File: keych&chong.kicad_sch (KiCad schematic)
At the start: 104 parts

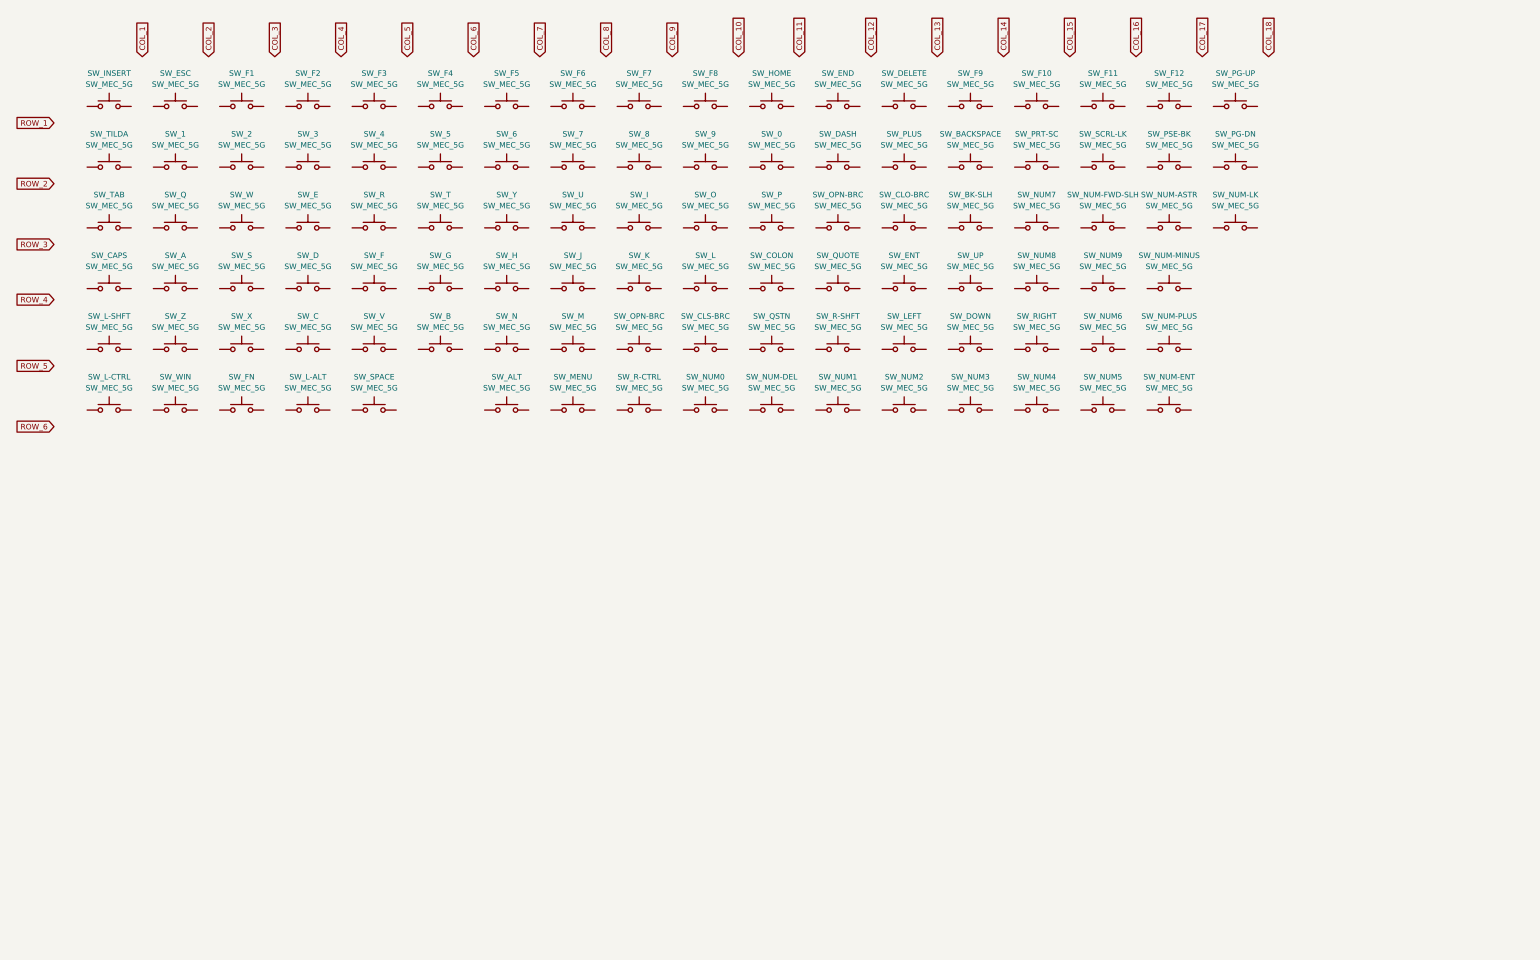
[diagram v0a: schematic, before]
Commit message: add connections to matrix schematic
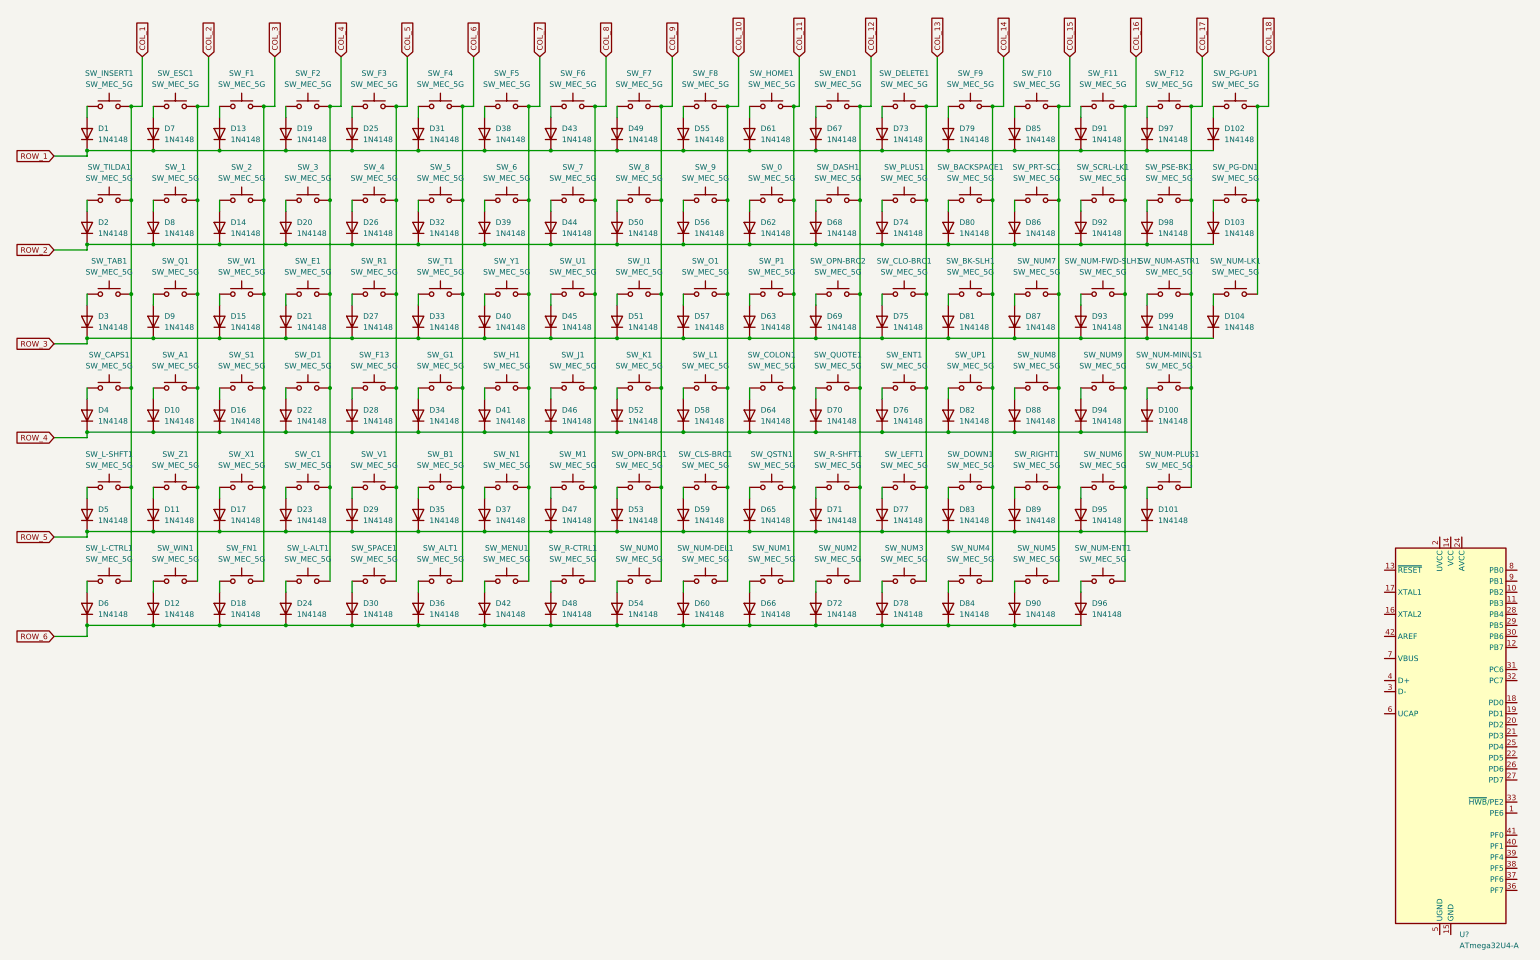
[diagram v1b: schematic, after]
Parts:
- added D1, D10, D100, D101, D102, D103, D104, D11, D12, D13, D14, D15, D16, D17, D18, D19, D2, D20, D21, D22, D23, D24, D25, D26, D27, D28, D29, D3, D30, D31, D32, D33, D34, D35, D36, D37, D38, D39, D4, D40, D41, D42, D43, D44, D45, D46, D47, D48, D49, D5, D50, D51, D52, D53, D54, D55, D56, D57, D58, D59, D6, D60, D61, D62, D63, D64, D65, D66, D67, D68, D69, D7, D70, D71, D72, D73, D74, D75, D76, D77, D78, D79, D8, D80, D81, D82, D83, D84, D85, D86, D87, D88, D89, D9, D90, D91, D92, D93, D94, D95, D96, D97, D98, D99: 1N4148, Diode_THT:D_DO-35_SOD27_P7.62mm_Horizontal, symbol Diode:1N4148
- added U?: ATmega32U4-A, Package_QFP:TQFP-44_10x10mm_P0.8mm, symbol MCU_Microchip_ATmega:ATmega32U4-A
- renumbered SW_A to SW_A1, SW_ALT to SW_ALT1, SW_B to SW_B1, SW_BACKSPACE to SW_BACKSPACE1, SW_BK-SLH to SW_BK-SLH1, SW_C to SW_C1, SW_CAPS to SW_CAPS1, SW_CLO-BRC to SW_CLO-BRC1, SW_CLS-BRC to SW_CLS-BRC1, SW_COLON to SW_COLON1, SW_D to SW_D1, SW_DASH to SW_DASH1, SW_DELETE to SW_DELETE1, SW_DOWN to SW_DOWN1, SW_E to SW_E1, SW_END to SW_END1, SW_ENT to SW_ENT1, SW_ESC to SW_ESC1, SW_F to SW_F13, SW_FN to SW_FN1, SW_G to SW_G1, SW_H to SW_H1, SW_HOME to SW_HOME1, SW_I to SW_I1, SW_INSERT to SW_INSERT1, SW_J to SW_J1, SW_K to SW_K1, SW_L-ALT to SW_L-ALT1, SW_L-CTRL to SW_L-CTRL1, SW_L-SHFT to SW_L-SHFT1, SW_L to SW_L1, SW_LEFT to SW_LEFT1, SW_M to SW_M1, SW_MENU to SW_MENU1, SW_N to SW_N1, SW_NUM-ASTR to SW_NUM-ASTR1, SW_NUM-DEL to SW_NUM-DEL1, SW_NUM-ENT to SW_NUM-ENT1, SW_NUM-FWD-SLH to SW_NUM-FWD-SLH1, SW_NUM-LK to SW_NUM-LK1, SW_NUM-MINUS to SW_NUM-MINUS1, SW_NUM-PLUS to SW_NUM-PLUS1, SW_O to SW_O1, SW_OPN-BRC to SW_OPN-BRC1, SW_OPN-BRC to SW_OPN-BRC2, SW_P to SW_P1, SW_PG-DN to SW_PG-DN1, SW_PG-UP to SW_PG-UP1, SW_PLUS to SW_PLUS1, SW_PRT-SC to SW_PRT-SC1, SW_PSE-BK to SW_PSE-BK1, SW_Q to SW_Q1, SW_QSTN to SW_QSTN1, SW_QUOTE to SW_QUOTE1, SW_R-CTRL to SW_R-CTRL1, SW_R-SHFT to SW_R-SHFT1, SW_R to SW_R1, SW_RIGHT to SW_RIGHT1, SW_S to SW_S1, SW_SCRL-LK to SW_SCRL-LK1, SW_SPACE to SW_SPACE1, SW_T to SW_T1, SW_TAB to SW_TAB1, SW_TILDA to SW_TILDA1, SW_U to SW_U1, SW_UP to SW_UP1, SW_V to SW_V1, SW_W to SW_W1, SW_WIN to SW_WIN1, SW_X to SW_X1, SW_Y to SW_Y1, SW_Z to SW_Z1
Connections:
- net COL_1: now also SW_CAPS1.3 (B), SW_CAPS1.4 (B), SW_INSERT1.3 (B), SW_INSERT1.4 (B), SW_L-CTRL1.3 (B), SW_L-CTRL1.4 (B), SW_L-SHFT1.3 (B), SW_L-SHFT1.4 (B), SW_TAB1.3 (B), SW_TAB1.4 (B), SW_TILDA1.3 (B), SW_TILDA1.4 (B)
- net COL_10: now also SW_9.3 (B), SW_9.4 (B), SW_CLS-BRC1.3 (B), SW_CLS-BRC1.4 (B), SW_F8.3 (B), SW_F8.4 (B), SW_L1.3 (B), SW_L1.4 (B), SW_NUM-DEL1.3 (B), SW_NUM-DEL1.4 (B), SW_O1.3 (B), SW_O1.4 (B)
- net COL_11: now also SW_0.3 (B), SW_0.4 (B), SW_COLON1.3 (B), SW_COLON1.4 (B), SW_HOME1.3 (B), SW_HOME1.4 (B), SW_NUM1.3 (B), SW_NUM1.4 (B), SW_P1.3 (B), SW_P1.4 (B), SW_QSTN1.3 (B), SW_QSTN1.4 (B)
- net COL_12: now also SW_DASH1.3 (B), SW_DASH1.4 (B), SW_END1.3 (B), SW_END1.4 (B), SW_NUM2.3 (B), SW_NUM2.4 (B), SW_OPN-BRC2.3 (B), SW_OPN-BRC2.4 (B), SW_QUOTE1.3 (B), SW_QUOTE1.4 (B), SW_R-SHFT1.3 (B), SW_R-SHFT1.4 (B)
- net COL_13: now also SW_CLO-BRC1.3 (B), SW_CLO-BRC1.4 (B), SW_DELETE1.3 (B), SW_DELETE1.4 (B), SW_ENT1.3 (B), SW_ENT1.4 (B), SW_LEFT1.3 (B), SW_LEFT1.4 (B), SW_NUM3.3 (B), SW_NUM3.4 (B), SW_PLUS1.3 (B), SW_PLUS1.4 (B)
- net COL_14: now also SW_BACKSPACE1.3 (B), SW_BACKSPACE1.4 (B), SW_BK-SLH1.3 (B), SW_BK-SLH1.4 (B), SW_DOWN1.3 (B), SW_DOWN1.4 (B), SW_F9.3 (B), SW_F9.4 (B), SW_NUM4.3 (B), SW_NUM4.4 (B), SW_UP1.3 (B), SW_UP1.4 (B)
- net COL_15: now also SW_F10.3 (B), SW_F10.4 (B), SW_NUM5.3 (B), SW_NUM5.4 (B), SW_NUM7.3 (B), SW_NUM7.4 (B), SW_NUM8.3 (B), SW_NUM8.4 (B), SW_PRT-SC1.3 (B), SW_PRT-SC1.4 (B), SW_RIGHT1.3 (B), SW_RIGHT1.4 (B)
- net COL_16: now also SW_F11.3 (B), SW_F11.4 (B), SW_NUM-ENT1.3 (B), SW_NUM-ENT1.4 (B), SW_NUM-FWD-SLH1.3 (B), SW_NUM-FWD-SLH1.4 (B), SW_NUM6.3 (B), SW_NUM6.4 (B), SW_NUM9.3 (B), SW_NUM9.4 (B), SW_SCRL-LK1.3 (B), SW_SCRL-LK1.4 (B)
- net COL_17: now also SW_F12.3 (B), SW_F12.4 (B), SW_NUM-ASTR1.3 (B), SW_NUM-ASTR1.4 (B), SW_NUM-MINUS1.3 (B), SW_NUM-MINUS1.4 (B), SW_NUM-PLUS1.3 (B), SW_NUM-PLUS1.4 (B), SW_PSE-BK1.3 (B), SW_PSE-BK1.4 (B)
- net COL_18: now also SW_NUM-LK1.3 (B), SW_NUM-LK1.4 (B), SW_PG-DN1.3 (B), SW_PG-DN1.4 (B), SW_PG-UP1.3 (B), SW_PG-UP1.4 (B)
- net COL_2: now also SW_1.3 (B), SW_1.4 (B), SW_A1.3 (B), SW_A1.4 (B), SW_ESC1.3 (B), SW_ESC1.4 (B), SW_Q1.3 (B), SW_Q1.4 (B), SW_WIN1.3 (B), SW_WIN1.4 (B), SW_Z1.3 (B), SW_Z1.4 (B)
- net COL_3: now also SW_2.3 (B), SW_2.4 (B), SW_F1.3 (B), SW_F1.4 (B), SW_FN1.3 (B), SW_FN1.4 (B), SW_S1.3 (B), SW_S1.4 (B), SW_W1.3 (B), SW_W1.4 (B), SW_X1.3 (B), SW_X1.4 (B)
- net COL_4: now also SW_3.3 (B), SW_3.4 (B), SW_C1.3 (B), SW_C1.4 (B), SW_D1.3 (B), SW_D1.4 (B), SW_E1.3 (B), SW_E1.4 (B), SW_F2.3 (B), SW_F2.4 (B), SW_L-ALT1.3 (B), SW_L-ALT1.4 (B)
- net COL_5: now also SW_4.3 (B), SW_4.4 (B), SW_F13.3 (B), SW_F13.4 (B), SW_F3.3 (B), SW_F3.4 (B), SW_R1.3 (B), SW_R1.4 (B), SW_SPACE1.3 (B), SW_SPACE1.4 (B), SW_V1.3 (B), SW_V1.4 (B)
- net COL_6: now also SW_5.3 (B), SW_5.4 (B), SW_ALT1.3 (B), SW_ALT1.4 (B), SW_B1.3 (B), SW_B1.4 (B), SW_F4.3 (B), SW_F4.4 (B), SW_G1.3 (B), SW_G1.4 (B), SW_T1.3 (B), SW_T1.4 (B)
- net COL_7: now also SW_6.3 (B), SW_6.4 (B), SW_F5.3 (B), SW_F5.4 (B), SW_H1.3 (B), SW_H1.4 (B), SW_MENU1.3 (B), SW_MENU1.4 (B), SW_N1.3 (B), SW_N1.4 (B), SW_Y1.3 (B), SW_Y1.4 (B)
- net COL_8: now also SW_7.3 (B), SW_7.4 (B), SW_F6.3 (B), SW_F6.4 (B), SW_J1.3 (B), SW_J1.4 (B), SW_M1.3 (B), SW_M1.4 (B), SW_R-CTRL1.3 (B), SW_R-CTRL1.4 (B), SW_U1.3 (B), SW_U1.4 (B)
- net COL_9: now also SW_8.3 (B), SW_8.4 (B), SW_F7.3 (B), SW_F7.4 (B), SW_I1.3 (B), SW_I1.4 (B), SW_K1.3 (B), SW_K1.4 (B), SW_NUM0.3 (B), SW_NUM0.4 (B), SW_OPN-BRC1.3 (B), SW_OPN-BRC1.4 (B)
- net ROW_1: now also D1.1 (K), D102.1 (K), D13.1 (K), D19.1 (K), D25.1 (K), D31.1 (K), D38.1 (K), D43.1 (K), D49.1 (K), D55.1 (K), D61.1 (K), D67.1 (K), D7.1 (K), D73.1 (K), D79.1 (K), D85.1 (K), D91.1 (K), D97.1 (K)
- net ROW_2: now also D103.1 (K), D14.1 (K), D2.1 (K), D20.1 (K), D26.1 (K), D32.1 (K), D39.1 (K), D44.1 (K), D50.1 (K), D56.1 (K), D62.1 (K), D68.1 (K), D74.1 (K), D8.1 (K), D80.1 (K), D86.1 (K), D92.1 (K), D98.1 (K)
- net ROW_3: now also D104.1 (K), D15.1 (K), D21.1 (K), D27.1 (K), D3.1 (K), D33.1 (K), D40.1 (K), D45.1 (K), D51.1 (K), D57.1 (K), D63.1 (K), D69.1 (K), D75.1 (K), D81.1 (K), D87.1 (K), D9.1 (K), D93.1 (K), D99.1 (K)
- net ROW_4: now also D10.1 (K), D100.1 (K), D16.1 (K), D22.1 (K), D28.1 (K), D34.1 (K), D4.1 (K), D41.1 (K), D46.1 (K), D52.1 (K), D58.1 (K), D64.1 (K), D70.1 (K), D76.1 (K), D82.1 (K), D88.1 (K), D94.1 (K)
- net ROW_5: now also D101.1 (K), D11.1 (K), D17.1 (K), D23.1 (K), D29.1 (K), D35.1 (K), D37.1 (K), D47.1 (K), D5.1 (K), D53.1 (K), D59.1 (K), D65.1 (K), D71.1 (K), D77.1 (K), D83.1 (K), D89.1 (K), D95.1 (K)
- net ROW_6: now also D12.1 (K), D18.1 (K), D24.1 (K), D30.1 (K), D36.1 (K), D42.1 (K), D48.1 (K), D54.1 (K), D6.1 (K), D60.1 (K), D66.1 (K), D72.1 (K), D78.1 (K), D84.1 (K), D90.1 (K), D96.1 (K)
- net at SW_DELETE1.1 (A), SW_DELETE1.2 (A): now also D73.2 (A)
- net at SW_Y1.1 (A), SW_Y1.2 (A): now also D40.2 (A)
- net at SW_G1.1 (A), SW_G1.2 (A): now also D34.2 (A)
- net at SW_X1.1 (A), SW_X1.2 (A): now also D17.2 (A)
- net at SW_SCRL-LK1.1 (A), SW_SCRL-LK1.2 (A): now also D92.2 (A)
- net at SW_END1.1 (A), SW_END1.2 (A): now also D67.2 (A)
- net at SW_NUM-PLUS1.1 (A), SW_NUM-PLUS1.2 (A): now also D101.2 (A)
- net at SW_4.1 (A), SW_4.2 (A): now also D26.2 (A)
- net at SW_INSERT1.1 (A), SW_INSERT1.2 (A): now also D1.2 (A)
- net at SW_OPN-BRC2.1 (A), SW_OPN-BRC2.2 (A): now also D69.2 (A)
- net at SW_NUM7.1 (A), SW_NUM7.2 (A): now also D87.2 (A)
- net at SW_F5.1 (A), SW_F5.2 (A): now also D38.2 (A)
- net at SW_L1.1 (A), SW_L1.2 (A): now also D58.2 (A)
- net at SW_B1.1 (A), SW_B1.2 (A): now also D35.2 (A)
- net at SW_DOWN1.1 (A), SW_DOWN1.2 (A): now also D83.2 (A)
- net at SW_TILDA1.1 (A), SW_TILDA1.2 (A): now also D2.2 (A)
- net at SW_D1.1 (A), SW_D1.2 (A): now also D22.2 (A)
- net at SW_Z1.1 (A), SW_Z1.2 (A): now also D11.2 (A)
- net at SW_1.1 (A), SW_1.2 (A): now also D8.2 (A)
- net at SW_F8.1 (A), SW_F8.2 (A): now also D55.2 (A)
- net at SW_R-SHFT1.1 (A), SW_R-SHFT1.2 (A): now also D71.2 (A)
- net at SW_OPN-BRC1.1 (A), SW_OPN-BRC1.2 (A): now also D53.2 (A)
- net at SW_H1.1 (A), SW_H1.2 (A): now also D41.2 (A)
- net at SW_RIGHT1.1 (A), SW_RIGHT1.2 (A): now also D89.2 (A)
- net at SW_NUM-MINUS1.1 (A), SW_NUM-MINUS1.2 (A): now also D100.2 (A)
- net at SW_COLON1.1 (A), SW_COLON1.2 (A): now also D64.2 (A)
- net at SW_L-CTRL1.1 (A), SW_L-CTRL1.2 (A): now also D6.2 (A)
- net at SW_PSE-BK1.1 (A), SW_PSE-BK1.2 (A): now also D98.2 (A)
- net at SW_CLS-BRC1.1 (A), SW_CLS-BRC1.2 (A): now also D59.2 (A)
- net at SW_7.1 (A), SW_7.2 (A): now also D44.2 (A)
- net at SW_UP1.1 (A), SW_UP1.2 (A): now also D82.2 (A)
- net at SW_F6.1 (A), SW_F6.2 (A): now also D43.2 (A)
- net at SW_F7.1 (A), SW_F7.2 (A): now also D49.2 (A)
- net at SW_FN1.1 (A), SW_FN1.2 (A): now also D18.2 (A)
- net at SW_LEFT1.1 (A), SW_LEFT1.2 (A): now also D77.2 (A)
- net at SW_F9.1 (A), SW_F9.2 (A): now also D79.2 (A)
- net at SW_PRT-SC1.1 (A), SW_PRT-SC1.2 (A): now also D86.2 (A)
- net at SW_C1.1 (A), SW_C1.2 (A): now also D23.2 (A)
- net at SW_NUM-DEL1.1 (A), SW_NUM-DEL1.2 (A): now also D60.2 (A)
- net at SW_F2.1 (A), SW_F2.2 (A): now also D19.2 (A)
- net at SW_F11.1 (A), SW_F11.2 (A): now also D91.2 (A)
- net at SW_9.1 (A), SW_9.2 (A): now also D56.2 (A)
- net at SW_E1.1 (A), SW_E1.2 (A): now also D21.2 (A)
- net at SW_PG-DN1.1 (A), SW_PG-DN1.2 (A): now also D103.2 (A)
- net at SW_I1.1 (A), SW_I1.2 (A): now also D51.2 (A)
- net at SW_K1.1 (A), SW_K1.2 (A): now also D52.2 (A)
- net at SW_F12.1 (A), SW_F12.2 (A): now also D97.2 (A)
- net at SW_PLUS1.1 (A), SW_PLUS1.2 (A): now also D74.2 (A)
- net at SW_BACKSPACE1.1 (A), SW_BACKSPACE1.2 (A): now also D80.2 (A)
- net at SW_NUM1.1 (A), SW_NUM1.2 (A): now also D66.2 (A)
- net at SW_2.1 (A), SW_2.2 (A): now also D14.2 (A)
- net at SW_QSTN1.1 (A), SW_QSTN1.2 (A): now also D65.2 (A)
- net at SW_BK-SLH1.1 (A), SW_BK-SLH1.2 (A): now also D81.2 (A)
- net at SW_ESC1.1 (A), SW_ESC1.2 (A): now also D7.2 (A)
- net at SW_NUM6.1 (A), SW_NUM6.2 (A): now also D95.2 (A)
- net at SW_0.1 (A), SW_0.2 (A): now also D62.2 (A)
- net at SW_3.1 (A), SW_3.2 (A): now also D20.2 (A)
- net at SW_P1.1 (A), SW_P1.2 (A): now also D63.2 (A)
- net at SW_QUOTE1.1 (A), SW_QUOTE1.2 (A): now also D70.2 (A)
- net at SW_PG-UP1.1 (A), SW_PG-UP1.2 (A): now also D102.2 (A)
- net at SW_A1.1 (A), SW_A1.2 (A): now also D10.2 (A)
- net at SW_F10.1 (A), SW_F10.2 (A): now also D85.2 (A)
- net at SW_U1.1 (A), SW_U1.2 (A): now also D45.2 (A)
- net at SW_R-CTRL1.1 (A), SW_R-CTRL1.2 (A): now also D48.2 (A)
- net at SW_SPACE1.1 (A), SW_SPACE1.2 (A): now also D30.2 (A)
- net at SW_S1.1 (A), SW_S1.2 (A): now also D16.2 (A)
- net at SW_CLO-BRC1.1 (A), SW_CLO-BRC1.2 (A): now also D75.2 (A)
- net at SW_NUM5.1 (A), SW_NUM5.2 (A): now also D90.2 (A)
- net at SW_NUM-FWD-SLH1.1 (A), SW_NUM-FWD-SLH1.2 (A): now also D93.2 (A)
- net at SW_MENU1.1 (A), SW_MENU1.2 (A): now also D42.2 (A)
- net at SW_M1.1 (A), SW_M1.2 (A): now also D47.2 (A)
- net at SW_ENT1.1 (A), SW_ENT1.2 (A): now also D76.2 (A)
- net at SW_N1.1 (A), SW_N1.2 (A): now also D37.2 (A)
- net at SW_R1.1 (A), SW_R1.2 (A): now also D27.2 (A)
- net at SW_NUM-LK1.1 (A), SW_NUM-LK1.2 (A): now also D104.2 (A)
- net at SW_V1.1 (A), SW_V1.2 (A): now also D29.2 (A)
- net at SW_8.1 (A), SW_8.2 (A): now also D50.2 (A)
- net at SW_NUM-ENT1.1 (A), SW_NUM-ENT1.2 (A): now also D96.2 (A)
- net at SW_T1.1 (A), SW_T1.2 (A): now also D33.2 (A)
- net at SW_NUM9.1 (A), SW_NUM9.2 (A): now also D94.2 (A)
- net at SW_J1.1 (A), SW_J1.2 (A): now also D46.2 (A)
- net at SW_F3.1 (A), SW_F3.2 (A): now also D25.2 (A)
- net at SW_NUM-ASTR1.1 (A), SW_NUM-ASTR1.2 (A): now also D99.2 (A)
- net at SW_NUM3.1 (A), SW_NUM3.2 (A): now also D78.2 (A)
- net at SW_ALT1.1 (A), SW_ALT1.2 (A): now also D36.2 (A)
- net at SW_TAB1.1 (A), SW_TAB1.2 (A): now also D3.2 (A)
- net at SW_DASH1.1 (A), SW_DASH1.2 (A): now also D68.2 (A)
- net at SW_NUM0.1 (A), SW_NUM0.2 (A): now also D54.2 (A)
- net at SW_F13.1 (A), SW_F13.2 (A): now also D28.2 (A)
- net at SW_HOME1.1 (A), SW_HOME1.2 (A): now also D61.2 (A)
- net at SW_5.1 (A), SW_5.2 (A): now also D32.2 (A)
- net at SW_F4.1 (A), SW_F4.2 (A): now also D31.2 (A)
- net at SW_L-SHFT1.1 (A), SW_L-SHFT1.2 (A): now also D5.2 (A)
- net at SW_6.1 (A), SW_6.2 (A): now also D39.2 (A)
- net at SW_CAPS1.1 (A), SW_CAPS1.2 (A): now also D4.2 (A)
- net at SW_NUM4.1 (A), SW_NUM4.2 (A): now also D84.2 (A)
- net at SW_W1.1 (A), SW_W1.2 (A): now also D15.2 (A)
- net at SW_L-ALT1.1 (A), SW_L-ALT1.2 (A): now also D24.2 (A)
- net at SW_Q1.1 (A), SW_Q1.2 (A): now also D9.2 (A)
- net at SW_F1.1 (A), SW_F1.2 (A): now also D13.2 (A)
- net at SW_NUM8.1 (A), SW_NUM8.2 (A): now also D88.2 (A)
- net at SW_NUM2.1 (A), SW_NUM2.2 (A): now also D72.2 (A)
- net at SW_WIN1.1 (A), SW_WIN1.2 (A): now also D12.2 (A)
- net at SW_O1.1 (A), SW_O1.2 (A): now also D57.2 (A)
- new net: U?.14 (VCC), U?.34 (VCC)
- new net: U?.15 (GND), U?.23 (GND), U?.35 (GND), U?.43 (GND)
- new net: U?.24 (AVCC), U?.44 (AVCC)
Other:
- moved on the sheet: SW_0, SW_1, SW_2, SW_3, SW_4, SW_5, SW_6, SW_7, SW_8, SW_9, SW_A1, SW_ALT1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

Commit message: updated matrix and added external crystal to schematic
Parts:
- added C? (x2): C, symbol Device:C
- added D? (x2): LED, symbol Device:LED
- added R? (x2): R, symbol Device:R
- added Y?: Crystal, symbol Device:Crystal
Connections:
- net ROW_1: no longer D102.1 (K), D97.1 (K)
- net ROW_2: no longer D103.1 (K), D98.1 (K)
- net ROW_3: no longer D104.1 (K), D99.1 (K)
- net ROW_4: no longer D100.1 (K)
- net ROW_5: no longer D101.1 (K)
- net at U?.16 (XTAL2): now also C?.2, Y?.1
- net at U?.17 (XTAL1): now also C?.2, Y?.2
- removed net COL_17: SW_F12.3 (B), SW_F12.4 (B), SW_NUM-ASTR1.3 (B), SW_NUM-ASTR1.4 (B), SW_NUM-MINUS1.3 (B), SW_NUM-MINUS1.4 (B), SW_NUM-PLUS1.3 (B), SW_NUM-PLUS1.4 (B), SW_PSE-BK1.3 (B), SW_PSE-BK1.4 (B)
- removed net COL_18: SW_NUM-LK1.3 (B), SW_NUM-LK1.4 (B), SW_PG-DN1.3 (B), SW_PG-DN1.4 (B), SW_PG-UP1.3 (B), SW_PG-UP1.4 (B)
- new net: SW_NUM-PLUS1.3 (B), SW_NUM-PLUS1.4 (B)
- new net: SW_NUM-MINUS1.3 (B), SW_NUM-MINUS1.4 (B)
- new net: C?.1, C?.1
- new net: SW_PSE-BK1.3 (B), SW_PSE-BK1.4 (B)
- new net: SW_PG-DN1.3 (B), SW_PG-DN1.4 (B)
- new net: SW_F12.3 (B), SW_F12.4 (B)
- new net: D?.2 (A), R?.2 (x2)
- new net: SW_PG-UP1.3 (B), SW_PG-UP1.4 (B)
- new net: SW_NUM-LK1.3 (B), SW_NUM-LK1.4 (B)
- new net: SW_NUM-ASTR1.3 (B), SW_NUM-ASTR1.4 (B)
- new net CAPS: R?.1
- new net GND: D?.1 (K), D?.1 (K)
- new net NUM: R?.1
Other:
- note added: "CAPS LED"
- note added: "NUM LED"
- moved on the sheet: D100, D101, D102, D103, D104, D97, D98, D99, SW_F12, SW_NUM-ASTR1, SW_NUM-LK1, SW_NUM-MINUS1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

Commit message: add decoupling capacitors to VCC
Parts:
- added C3: 1µF, symbol Device:C
- added C4, C5, C6, C?: 0.1µF, symbol Device:C
- added C7: 10µF, symbol Device:C_Polarized
- C1, C2: renamed from C?; value C -> 22pf
- gave numbers to parts that had none: 6
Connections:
- net GND is gone; now on net GNDREF: D105.1 (K), D106.1 (K)
- net GNDREF: now reaches C1.1, C2.1
- net GNDREF: now also C3.2, C4.2, C5.2, C6.2, C7.2, C?.2
- net at U1.6 (UCAP): now also C3.1
- new net VCC: C4.1, C5.1, C6.1, C7.1, C?.1

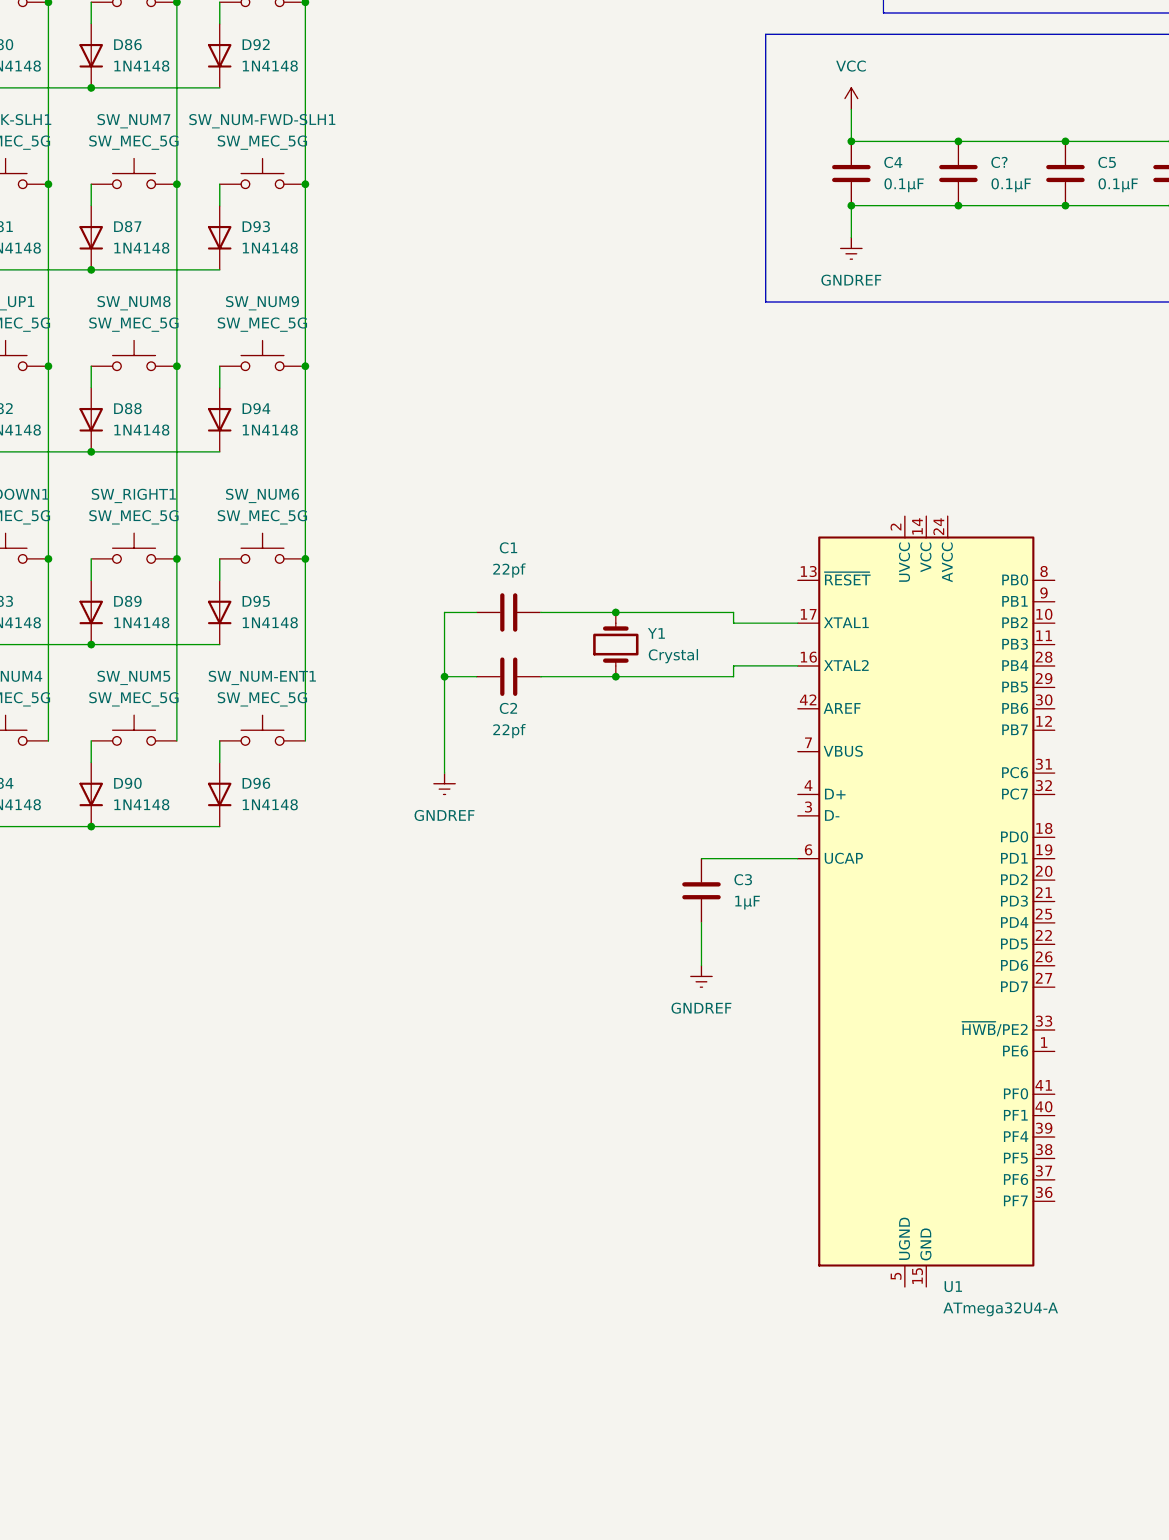
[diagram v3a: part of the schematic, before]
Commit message: add usb c to schematic
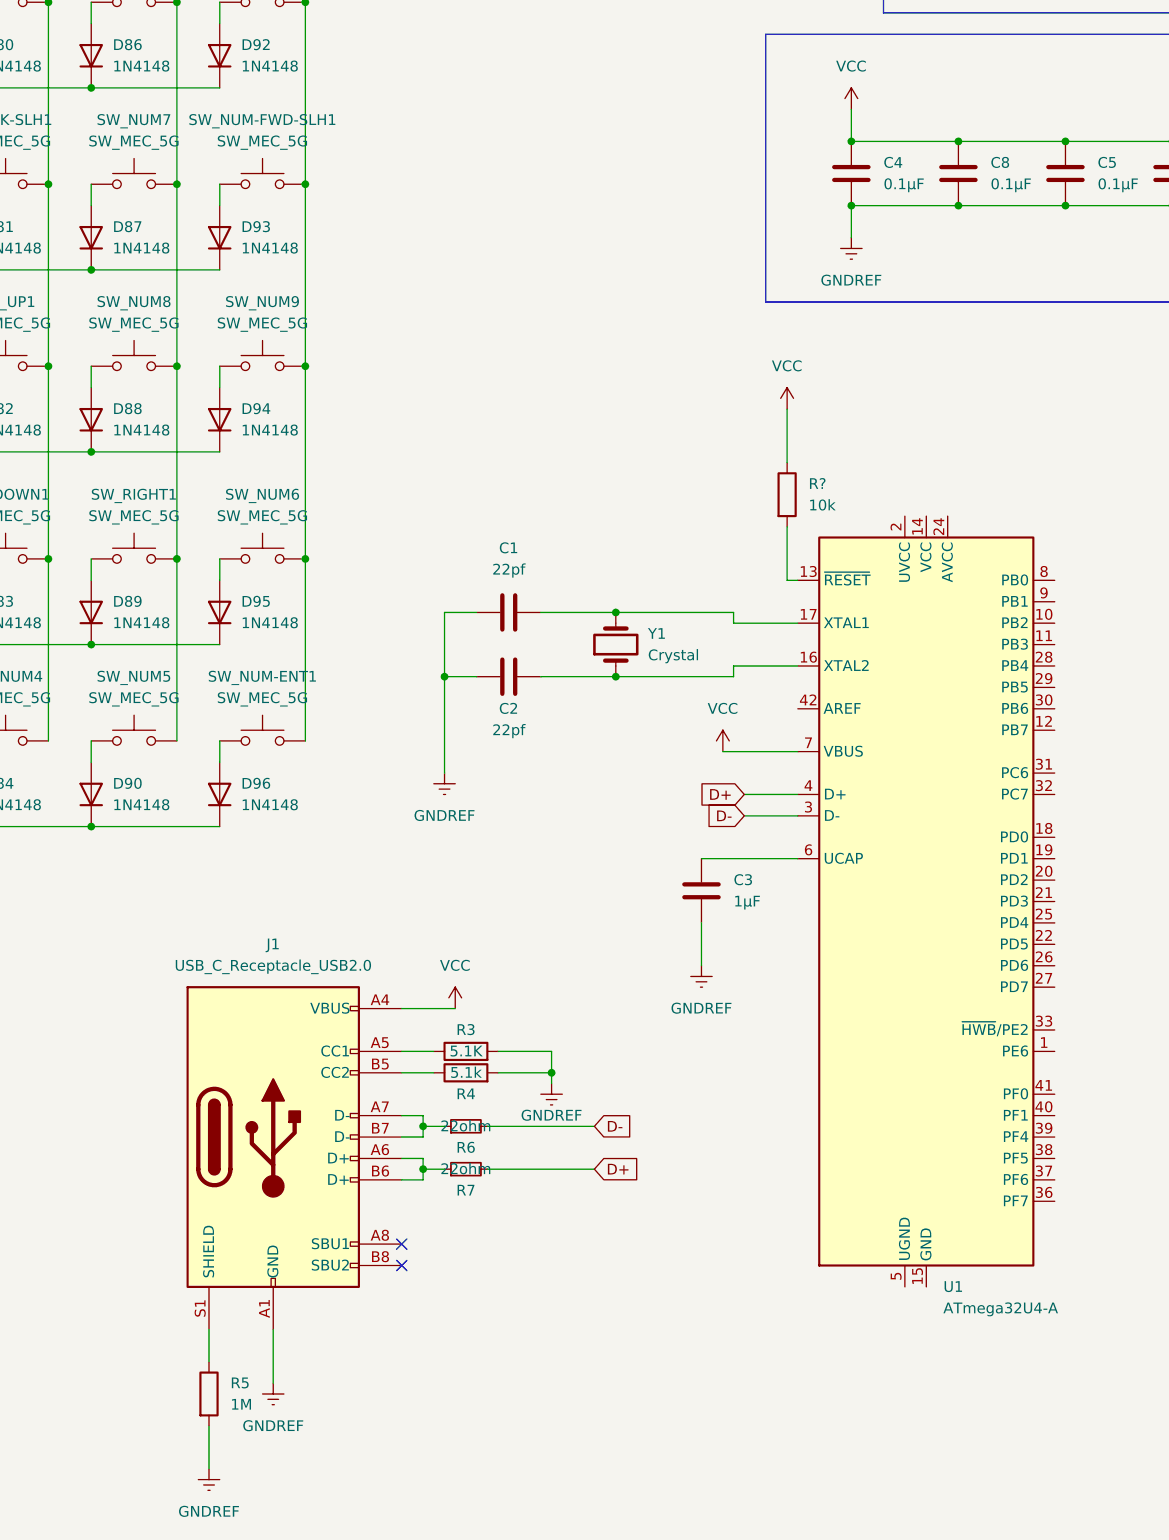
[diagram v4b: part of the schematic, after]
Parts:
- added J1: USB_C_Receptacle_USB2.0, symbol Connector:USB_C_Receptacle_USB2.0
- added R3: 5.1K, symbol Device:R
- added R4: 5.1k, symbol Device:R
- added R5: 1M, symbol Device:R
- added R6, R7: 22ohm, symbol Device:R_Small
- added R?: 10k, symbol Device:R
- gave numbers to parts that had none: 1
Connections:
- net GNDREF: now also J1.A1 (GND), J1.A12 (GND), J1.B1 (GND), J1.B12 (GND), R3.2, R4.2, R5.2
- net VCC: now also U1.7 (VBUS), J1.A4 (VBUS), J1.A9 (VBUS), J1.B4 (VBUS), J1.B9 (VBUS), R?.1
- net at U1.13 (~{RESET}): now also R?.2
- net D-: now reaches U1.3 (D-)
- net D-: now also R6.2
- net D+: now reaches U1.4 (D+)
- net D+: now also R7.2
- new net: J1.A5 (CC1), R3.1
- new net: J1.A7 (D-), J1.B7 (D-), R6.1
- new net: J1.S1 (SHIELD), R5.1
- new net: J1.B5 (CC2), R4.1
- new net: J1.A6 (D+), J1.B6 (D+), R7.1
- no-connect marks 0 -> 2
